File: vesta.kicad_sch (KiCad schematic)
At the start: 60 parts, among them J1 Solar Panel, J2 Solar Panel, J3 Conn_ARM_SWD_TagConnect_TC203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, J4 U.FL, U1 STM32WL55CCU6, U2 BQ24074RGTR, U3 TPS63900DSKR, U4 BME688_C3664478, U6 PE4259-63, X1 Q13FC1350000400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

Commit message: feat: adding all the footprints
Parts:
- removed L1: 2.2uH, symbol Device:L
- removed L2: 15uH, symbol Device:L
- removed Y1: 32MHz, symbol Device:Crystal
- added L1: FTC252012S2R2MBCA, JLCImport:FTC252012S2R2MBCA, symbol JLCImport:FTC252012S2R2MBCA
- added L3: FNR5040S150MT, JLCImport:FNR5040S150MT, symbol JLCImport:FNR5040S150MT
- added X2: X201632MMB4SI, JLCImport:X201632MMB4SI, symbol JLCImport:X201632MMB4SI
- C1: footprint (none) -> Capacitor_SMD:C_0805_2012Metric
- C10, C11, C12, C13, C15, C19, C22, C23, C7, C8, C9: footprint (none) -> PCM_JLCPCB:C_0603
- C14, C3, C4, C5, C6: footprint (none) -> PCM_JLCPCB:C_0805
- C16, C17, C18: footprint (none) -> PCM_JLCPCB:C_0402
- C2, C20, C21: footprint (none) -> Capacitor_SMD:C_0603_1608Metric
- D1: footprint (none) -> Diode_SMD:D_SOD-123
- J1, J2: footprint (none) -> JLCImport:WAFER-PH2_0-2PWZ
- JP_TMR_DISABLE1: renamed from JP_TMR_DISABLE; footprint (none) -> Jumper:SolderJumper-2_P1.3mm_Open_RoundedPad1.0x1.5mm
- R1, R10, R12, R14, R15, R16, R2, R3, R4, R5, R6, R7, R8, R9: footprint (none) -> PCM_JLCPCB:R_0603
- R11, R13: footprint (none) -> PCM_JLCPCB:R_0402
- TP1: footprint (none) -> TestPoint:TestPoint_Pad_D1.5mm
- TP2, TP3: footprint (none) -> TestPoint:TestPoint_Pad_D1.0mm
- renumbered BATTERY to BATTERY1, J_EXP to J_EXP1
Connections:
- net GND: now also X2.2 (GND), X2.4 (GND)
- net OSC_IN: now also X2.1 (OSC1)
- net OSC_OUT: now also X2.3 (OSC2)
- net SMPS_1V55: now also L3.2
- net at U3.9 (LX1): now also L1.1
- net at U3.7 (LX2): now also L1.2

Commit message: feat: making the pinecone
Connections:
- no-connect marks 1 -> 16

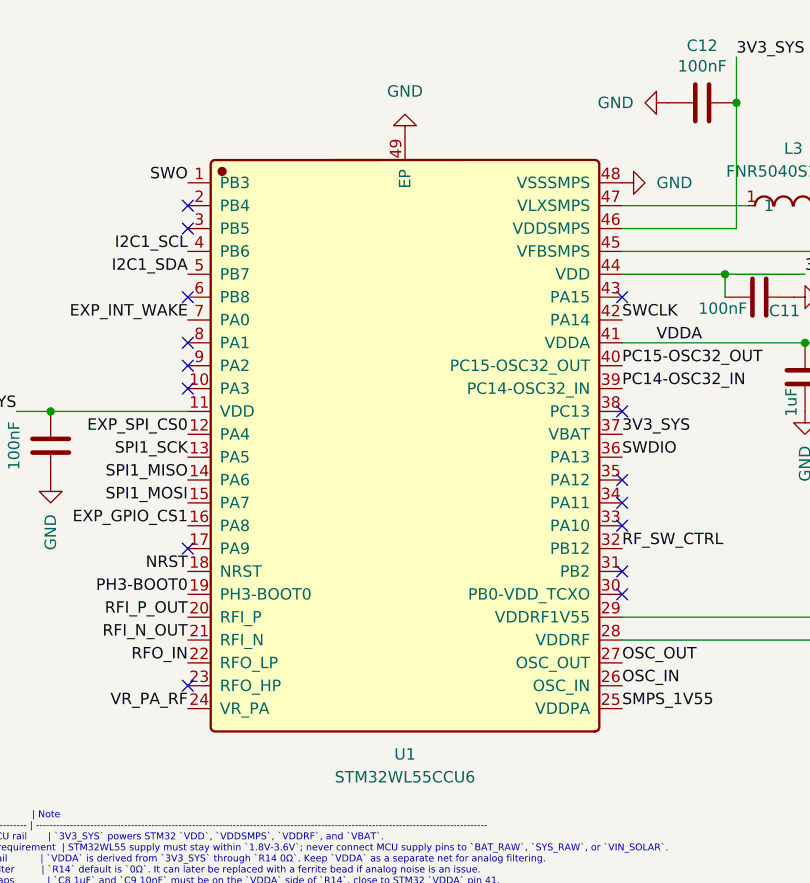
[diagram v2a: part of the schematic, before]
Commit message: feat: updating the pins in the stm32 footprint
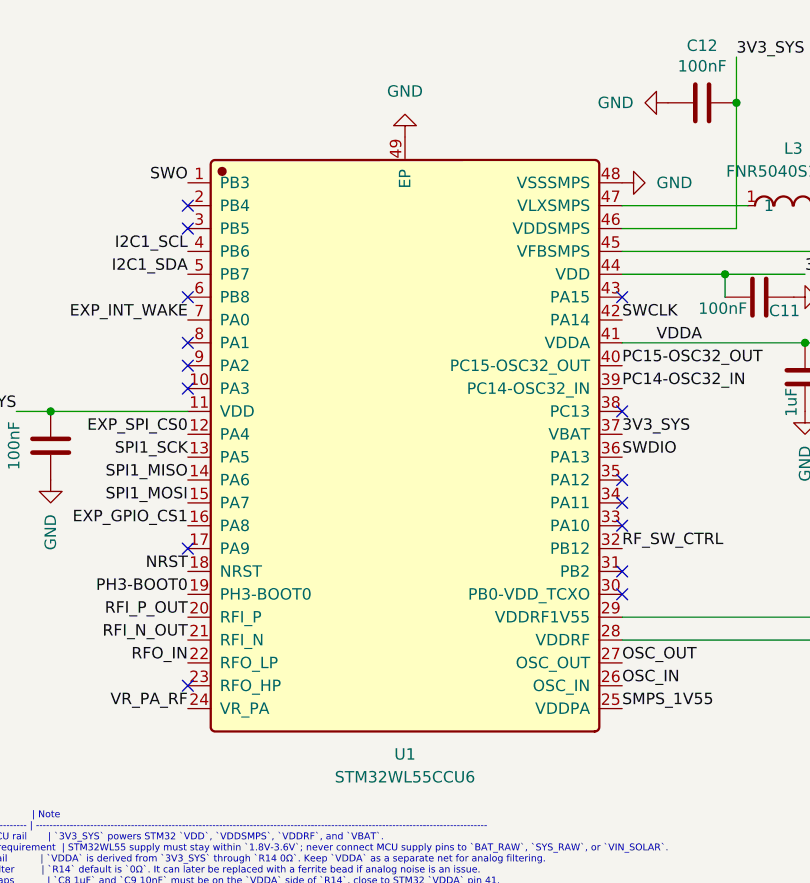
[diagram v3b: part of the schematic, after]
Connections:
- net GND: now also U1.48 (VSSSMPS)
- net OSC_IN: now also U1.26 (OSC_IN)
- net SMPS_1V55: now also U1.25 (VDDPA)
- net SWO: now also U1.1 (PB3)
- net VR_PA_RF: now also U1.24 (VR_PA)
- net at L3.1: now also U1.47 (VLXSMPS)
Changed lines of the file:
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@@
+		)
+	)
+	(label "OSC_IN"
+		(at 104.14 96.52 0)
+		(effects
+			(font
+				(size 1.27 1.27)
+			)
+			(justify left bottom)
 		)
 	)
@@
 		)
 	)
-	(label "OSC_IN"
-		(at 104.14 96.52 0)
-		(effects
-			(font
-				(size 1.27 1.27)
-			)
-			(justify left bottom)
-		)
-	)

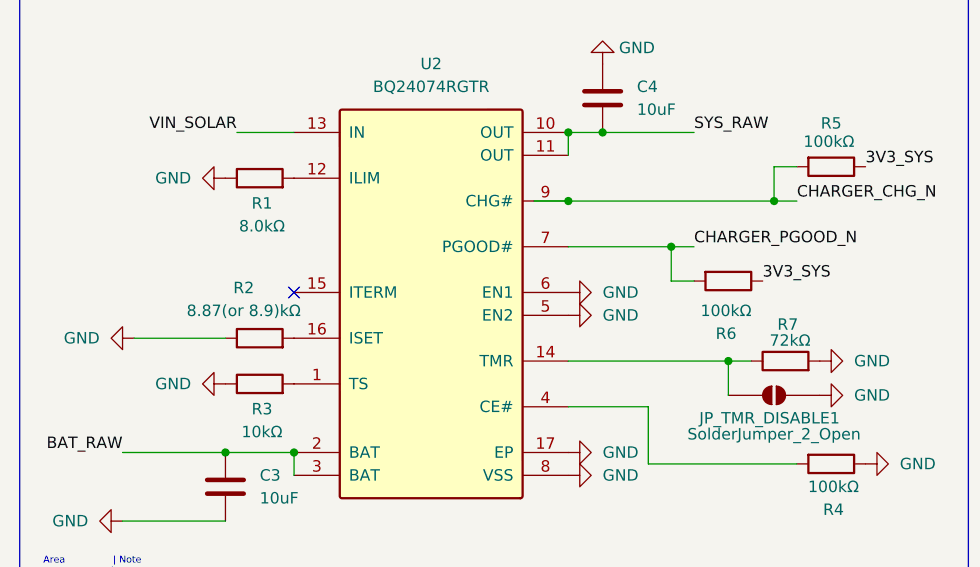
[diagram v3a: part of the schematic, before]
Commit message: feat: improving the thermal dissipation of the sensor
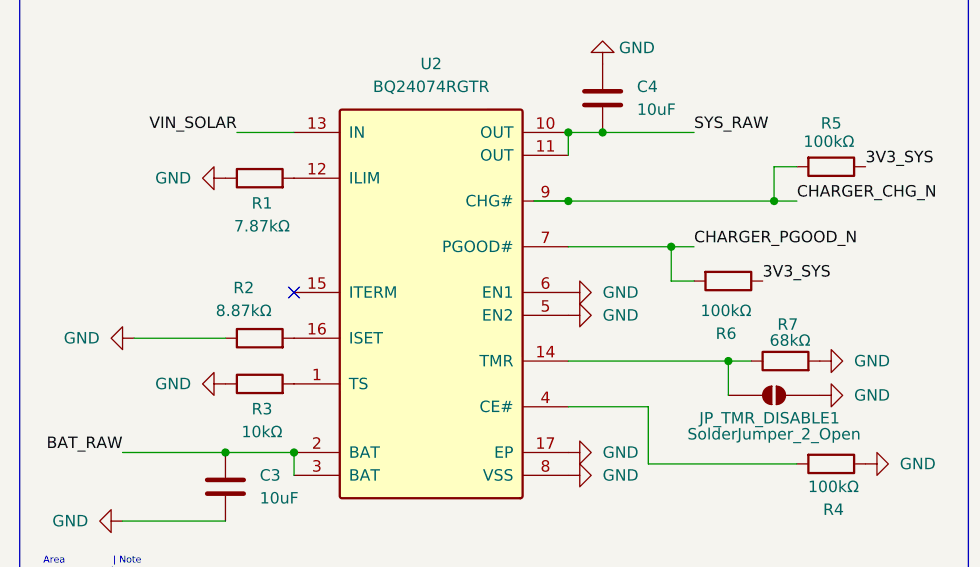
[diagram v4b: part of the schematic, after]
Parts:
- J_EXP1: footprint Connector_PinHeader_1.00mm:PinHeader_1x10_P1.00mm_Horizontal -> Connector_PinHeader_2.00mm:PinHeader_1x10_P2.00mm_Vertical
- R1: value 8.0kΩ -> 7.87kΩ
- R2: value 8.87(or 8.9)kΩ -> 8.87kΩ
- R7: value 72kΩ -> 68kΩ
- TP1, TP2, TP3: now left out of the parts list
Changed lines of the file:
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@@
 		(body_style 1)
 		(exclude_from_sim no)
-		(in_bom yes)
+		(in_bom no)
 		(on_board yes)
-		(in_pos_files yes)
+		(in_pos_files no)
 		(dnp no)
 		(property "Reference" "TP1"
@@
 			)
 		)
-		(property "Value" "8.0kΩ"
+		(property "Value" "7.87kΩ"
 			(at 297.434 87.884 90)
 			(show_name no)
@@
 		(body_style 1)
 		(exclude_from_sim no)
-		(in_bom yes)
+		(in_bom no)
 		(on_board yes)
-		(in_pos_files yes)
+		(in_pos_files no)
 		(dnp no)
 		(property "Reference" "TP2"
@@
 		(body_style 1)
 		(exclude_from_sim no)
-		(in_bom yes)
+		(in_bom no)
 		(on_board yes)
-		(in_pos_files yes)
+		(in_pos_files no)
 		(dnp no)
 		(fields_autoplaced yes)
@@
 			)
 		)
-		(property "Value" "8.87(or 8.9)kΩ"
+		(property "Value" "8.87kΩ"
 			(at 295.402 97.282 90)
 			(show_name no)
@@
 			)
 		)
-		(property "Footprint" "Connector_PinHeader_1.00mm:PinHeader_1x10_P1.00mm_Horizontal"
+		(property "Footprint" "Connector_PinHeader_2.00mm:PinHeader_1x10_P2.00mm_Vertical"
 			(at 231.14 154.94 0)
 			(hide yes)
@@
 			)
 		)
-		(property "Value" "72kΩ"
+		(property "Value" "68kΩ"
 			(at 356.108 100.584 90)
 			(show_name no)
